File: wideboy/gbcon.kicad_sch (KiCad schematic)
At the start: 36 parts, among them CN3 Conn_02x20_Odd_Even, CN4 GBA_ELP, CN5 GBA-CART-CONN, CN6 Conn_01x02, CN7 GBA_ELP, U12 CPU-AGB

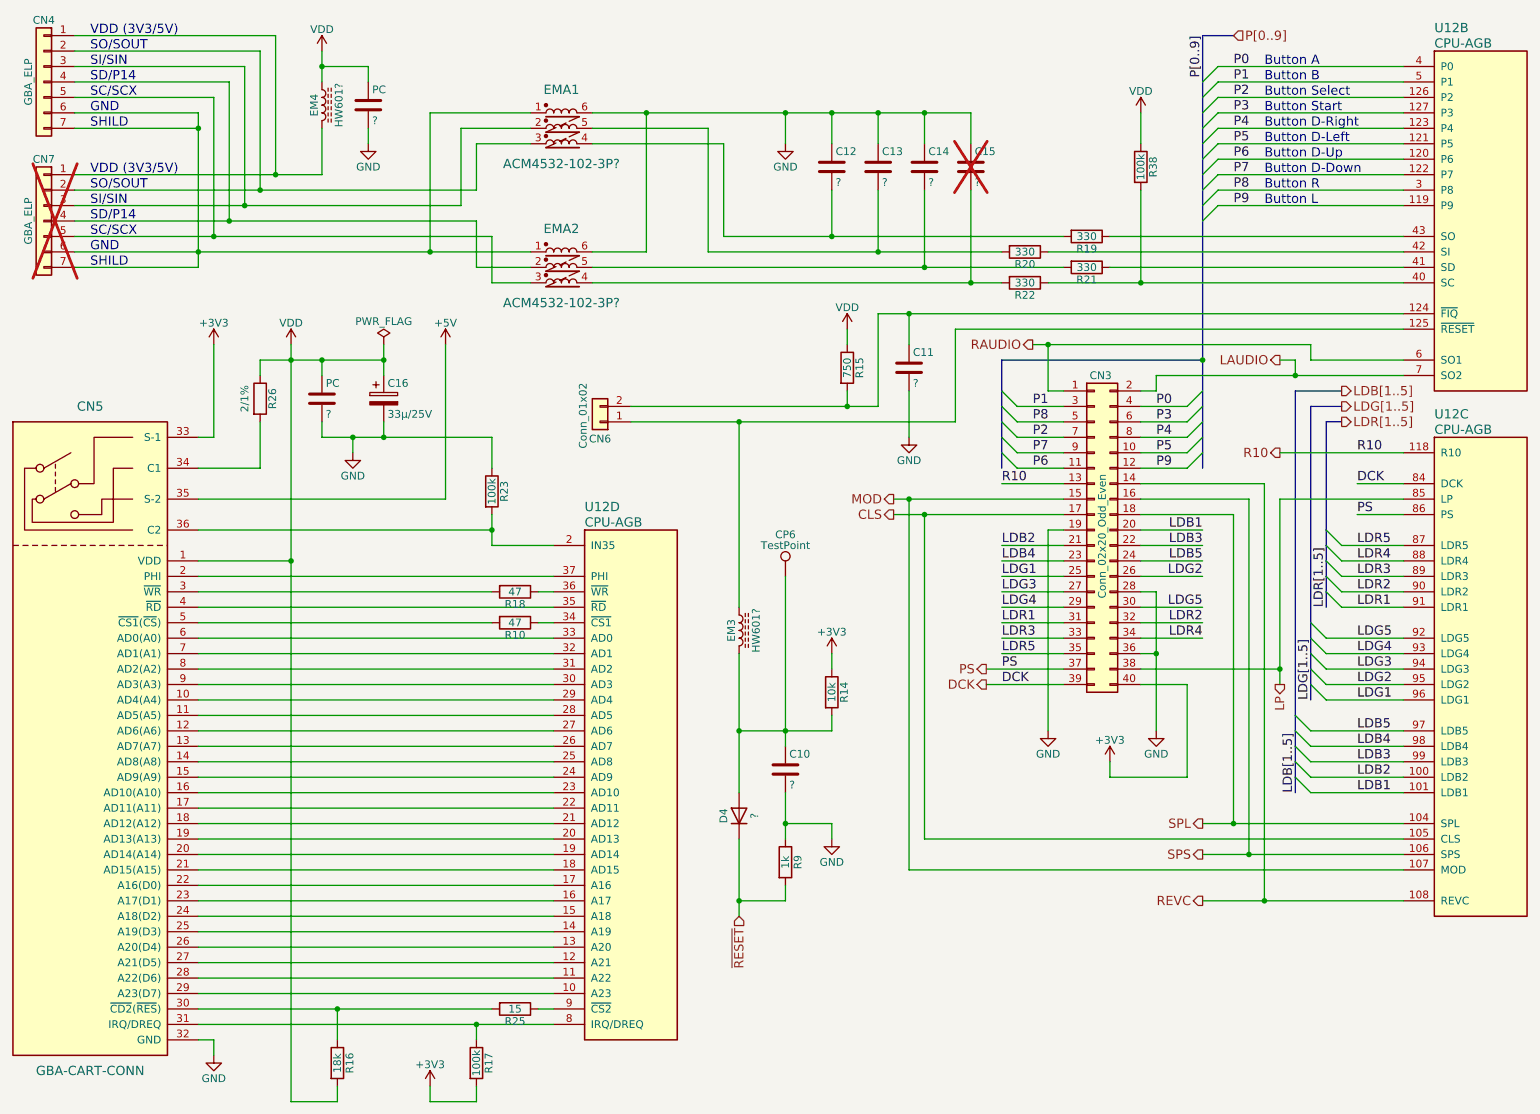
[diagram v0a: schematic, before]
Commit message: Add values for capacitors and diodes
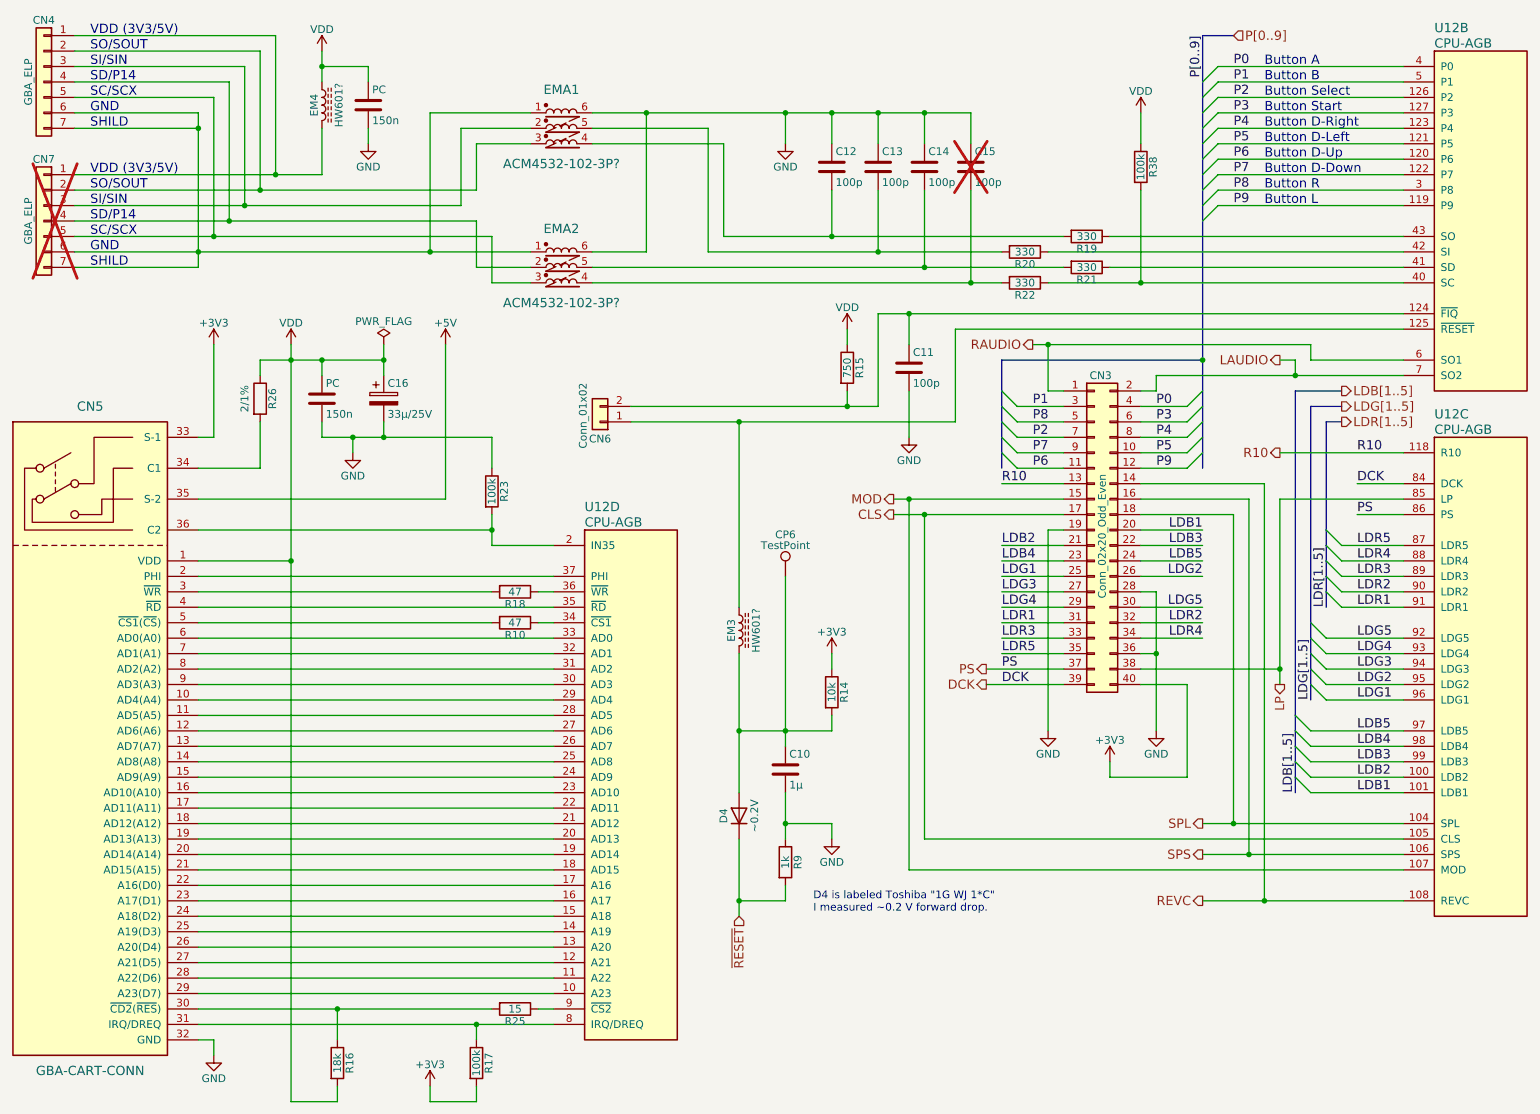
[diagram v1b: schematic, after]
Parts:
- C10: value ? -> 1µ
- C11, C12, C13, C14, C15: value ? -> 100p
- D4: value ? -> ~0.2V
- PC: value ? -> 150n
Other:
- note added: "D4 is labeled Toshiba "1G WJ 1*C" I measured ~0.2 V forward drop."
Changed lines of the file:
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@@
 	(title_block
 		(title "Wide-Boy64 AGB")
-		(date "2024-06-20")
-		(rev "2")
+		(date "2024-09-22")
+		(rev "3")
 		(company "CC-BY-SA-4.0 Michael Singer")
 		(comment 1 "https://github.com/msinger/wideboy/")
@@
 		)
 	)
+	(text "D4 is labeled Toshiba \"1G WJ 1*C\"\nI measured ~0.2 V forward drop."
+		(exclude_from_sim no)
+		(at 151.892 160.274 0)
+		(effects
+			(font
+				(size 1.27 1.27)
+			)
+			(justify left)
+		)
+	)
 	(text "SO/SOUT"
 		(exclude_from_sim no)
@@
 			)
 		)
-		(property "Value" "?"
+		(property "Value" "150n"
 			(at 71.755 80.01 0)
 			(effects
@@
 			)
 		)
-		(property "Value" "?"
+		(property "Value" "100p"
 			(at 178.435 41.91 0)
 			(effects
@@
 			)
 		)
-		(property "Value" "?"
+		(property "Value" "100p"
 			(at 170.815 41.91 0)
 			(effects
@@
 			)
 		)
-		(property "Value" "?"
+		(property "Value" "100p"
 			(at 163.195 41.91 0)
 			(effects
@@
 			)
 		)
-		(property "Value" "?"
+		(property "Value" "100p"
 			(at 155.575 41.91 0)
 			(effects
@@
 			)
 		)
-		(property "Value" "?"
+		(property "Value" "100p"
 			(at 168.275 74.93 0)
 			(effects
@@
 			)
 		)
-		(property "Value" "?"
+		(property "Value" "150n"
 			(at 79.375 31.75 0)
 			(effects
@@
 			)
 		)
-		(property "Value" "?"
+		(property "Value" "~0.2V"
 			(at 142.24 146.05 0)
 			(effects
@@
 			)
 		)
-		(property "Value" "?"
+		(property "Value" "1µ"
 			(at 147.955 140.97 0)
 			(effects
